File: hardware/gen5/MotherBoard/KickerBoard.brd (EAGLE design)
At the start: 141.6 x 141.1 mm, 154 parts, among them U1 SAM3S4B

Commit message: More motherboard work!
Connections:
- removed net N$39: MOTOR2.15, MOTOR2.16, MOTOR2.17, MOTOR2.18, U$8.6, U$8.7
- net 12VGND: now also MOTOR1.22, MOTOR1.33, MOTOR1.34, MOTOR2.15, MOTOR2.16, MOTOR2.17, MOTOR2.18, MOTOR2.22, MOTOR2.33, MOTOR2.34, MOTOR3.22, MOTOR3.33, MOTOR3.34, MOTOR4.22, MOTOR4.33, MOTOR4.34, U$10.5, U$11.5, U$8.6, U$8.7, U$9.5
- net GND: no longer MOTOR1.22, MOTOR1.33, MOTOR1.34, MOTOR2.22, MOTOR2.33, MOTOR2.34, MOTOR3.22, MOTOR3.33, MOTOR3.34, MOTOR4.22, MOTOR4.33, MOTOR4.34, U$10.5, U$11.5, U$9.5
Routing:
- net FAULT0: track 0.00 -> 109.2 mm, vias 0 -> 4
- net FAULT3: track 0.00 -> 106.2 mm, vias 0 -> 6
- net DIR0: track 0.00 -> 103.3 mm, vias 0 -> 4
- net 3.3V: track 274.5 -> 370.2 mm, vias 0 -> 6
- net BREN0: track 0.00 -> 76.9 mm, vias 0 -> 2
- net DIR1: track 0.00 -> 75.6 mm, vias 0 -> 2
- net GND: track 123.5 -> 186.3 mm, vias 13 -> 22
- net 12VGND: track 128.2 -> 187.4 mm, vias 5 -> 9
- net BREN1: track 0.00 -> 58.3 mm, vias 0 -> 4
- net DIR2: track 0.00 -> 53.1 mm, vias 0 -> 4
- net BREN3: track 0.00 -> 47.5 mm
- net PWM0: track 0.00 -> 44.4 mm, vias 0 -> 2
- net DIVCAP: track 6.75 -> 47.0 mm, vias 0 -> 4
- net DIR3: track 0.00 -> 38.5 mm
- net PWM3: track 0.00 -> 37.7 mm
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
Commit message: More Motherboard layout progress
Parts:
- moved C27 2.09 mm to (55.2, 46.0)
- moved C22 2.09 mm to (51.9, 46.4)
- moved C24 2.09 mm to (50.2, 46.4)
- moved C25 2.09 mm to (48.5, 46.4)
- moved C26 2.09 mm to (53.5, 46.0)
- moved R34 0.10 mm to (82.8, 48.0)
- moved R35 0.05 mm to (82.8, 50.1)
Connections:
- removed net M0QA: U1.42
- removed net M0QB: U1.41
- removed net M1QA: U1.37
- removed net M1QB: U1.38
- removed net M2QA: U1.25
- removed net M2QB: U1.26
- removed net M3QA: U1.52
- removed net M3QB: U1.23
- net M1QA-1: now also U1.25
- net M1QA-2: now also U1.37
- net M1QA-3: now also U1.42
- net M1QA-4: now also U1.52
- net M1QB-1: now also U1.26
- net M1QB-2: now also U1.38
- net M1QB-3: now also U1.41
- net M1QB-4: now also U1.23
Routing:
- net M1QA-2: track 0.00 -> 57.4 mm, vias 0 -> 4
- net M1QB-2: track 0.00 -> 55.3 mm, vias 0 -> 4
- net M1QB-3: track 0.00 -> 24.4 mm, vias 0 -> 2
- net FAULT: track 0.00 -> 23.0 mm, vias 0 -> 2
- net M1QA-3: track 0.00 -> 21.4 mm, vias 0 -> 2
- net 3.3V: track 370.2 -> 377.3 mm
- net PWM2: track 34.1 -> 40.4 mm
- net BREN2: track 37.6 -> 40.9 mm
- net TWCK: track 8.08 -> 10.6 mm
- net TWD: track 8.14 -> 9.15 mm

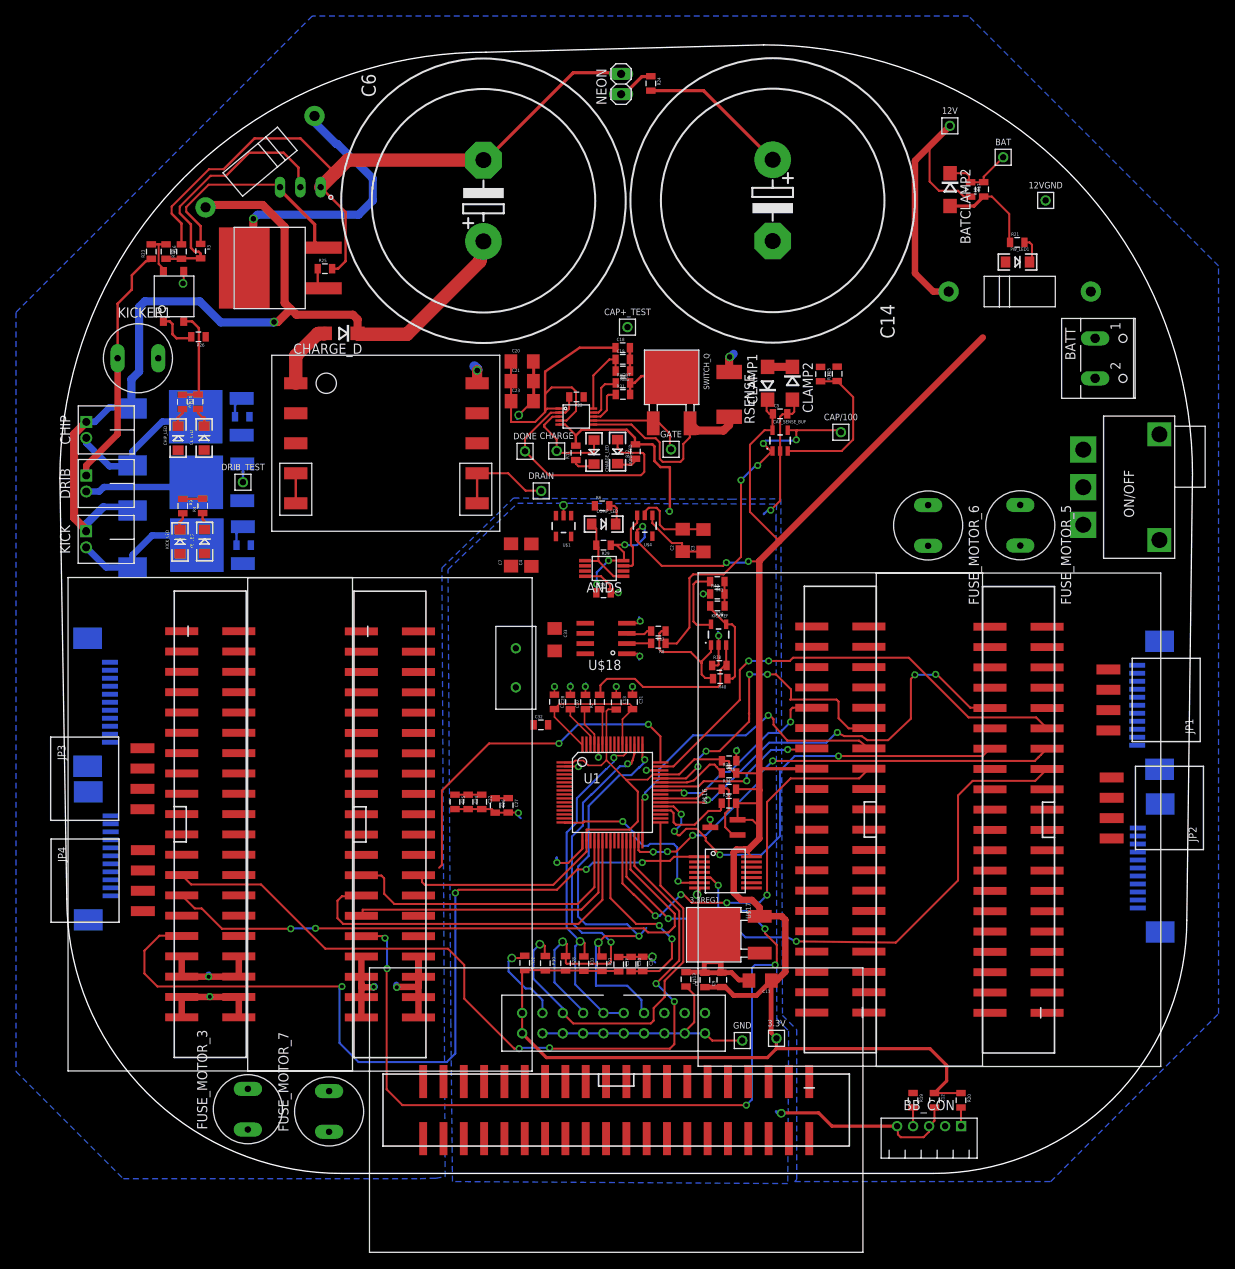
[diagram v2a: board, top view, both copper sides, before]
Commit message: Finishing up layout out traces for MCU on Motherboard
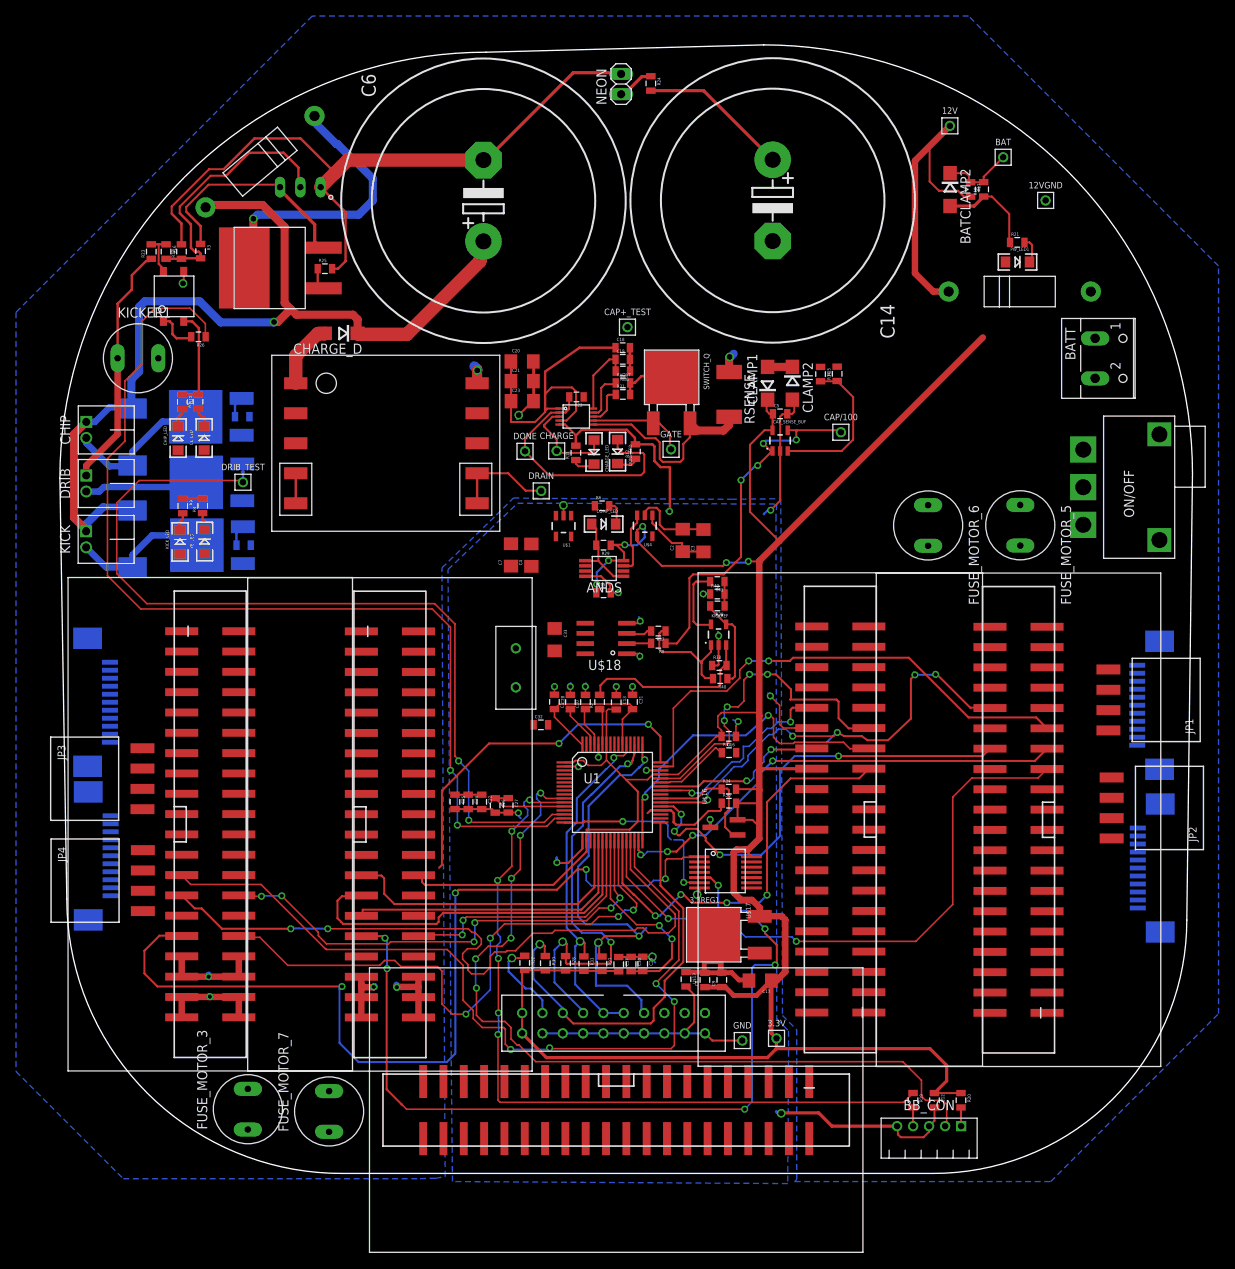
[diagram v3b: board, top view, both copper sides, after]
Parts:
- moved C16 3.05 mm to (82.7, 54.6)
- moved R35 2.54 mm to (82.8, 52.6)
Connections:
- net TWCK: now also COM_BOARD.17
- net TWD: now also COM_BOARD.19
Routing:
- net DISCHARGE: track 0.00 -> 129.2 mm, vias 0 -> 2
- net DRIB: track 2.33 -> 110.8 mm, vias 0 -> 2
- net BB_IN: track 0.00 -> 104.3 mm, vias 0 -> 6
- net BB_OUT: track 0.00 -> 97.2 mm, vias 0 -> 6
- net M1QB-1: track 0.00 -> 75.3 mm, vias 0 -> 4
- net M1QA-1: track 0.00 -> 61.6 mm, vias 0 -> 6
- net M1QB-4: track 0.00 -> 33.5 mm, vias 0 -> 2
- net BREN0: track 76.9 -> 88.5 mm
- net GND: track 186.3 -> 195.9 mm, vias 22 -> 23
- net VDDOUT: track 48.2 -> 57.6 mm
- net 12VGND: track 187.4 -> 178.5 mm
- net TWCK: track 10.6 -> 18.9 mm
- net FAULT0: track 109.2 -> 113.0 mm
- net 3.3V: track 377.3 -> 380.8 mm
- net M1QB-2: track 55.3 -> 58.8 mm, vias 4 -> 5
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
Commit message: Motherboard progress
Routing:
- net CHARGE: track 12.5 -> 80.8 mm, vias 0 -> 3
- net FAULT1: track 0.00 -> 60.0 mm, vias 0 -> 6
- net TWD: track 9.71 -> 69.5 mm, vias 0 -> 4
- net CHARGE_DONE: track 33.4 -> 91.3 mm, vias 0 -> 2
- net FAULT2: track 0.00 -> 51.4 mm, vias 0 -> 4
- net TWCK: track 18.9 -> 66.4 mm, vias 0 -> 2
- net M1QA-4: track 0.00 -> 41.6 mm, vias 0 -> 2
- net PWM0: track 44.4 -> 79.9 mm, vias 2 -> 4
- net VDDOUT: track 57.6 -> 78.9 mm, vias 2 -> 4
- net N$34: track 3.34 -> 14.6 mm
- net TDO: track 57.3 -> 52.4 mm
- net BREN1: track 58.8 -> 62.4 mm
- net TDI: track 52.0 -> 55.3 mm
- net BREN2: track 42.0 -> 44.1 mm
- net M1QB-1: track 75.3 -> 73.7 mm
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
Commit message: More motherboard Progress
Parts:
- moved FUSE_MOTOR_3 64.4 mm to (4.83, 69.9), turned to 0 degrees
- moved FUSE_MOTOR_7 62.3 mm to (29.1, 70.0), turned to 0 degrees
- moved C32 0.71 mm to (59.2, 55.4)
- moved C10 0.51 mm to (64.8, 59.4)
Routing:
- net 12V: track 79.4 -> 385.1 mm
- net GND: track 197.3 -> 304.8 mm, vias 23 -> 32
- net 3.3V: track 380.4 -> 485.1 mm, vias 8 -> 11
- net N$63: track 0.00 -> 61.0 mm, vias 0 -> 1
- net N$25: track 0.00 -> 60.4 mm
- net N$64: track 0.00 -> 58.1 mm, vias 0 -> 1
- net N$62: track 0.00 -> 57.6 mm, vias 0 -> 1
- net N$27: track 0.00 -> 55.9 mm
- net CHIP_ENABLE: track 0.00 -> 55.1 mm, vias 0 -> 2
- net M1QB-4: track 33.5 -> 88.4 mm, vias 2 -> 4
- net N$66: track 0.00 -> 47.4 mm, vias 0 -> 1
- net N$69: track 0.00 -> 45.2 mm, vias 0 -> 1
- net KICK_ENABLE: track 0.00 -> 44.3 mm, vias 0 -> 4
- net M1QA-4: track 41.6 -> 84.4 mm, vias 2 -> 4
- net N$68: track 0.00 -> 42.8 mm, vias 0 -> 1
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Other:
- board size 141.6 x 141.1 mm -> 141.6 x 142.1 mm

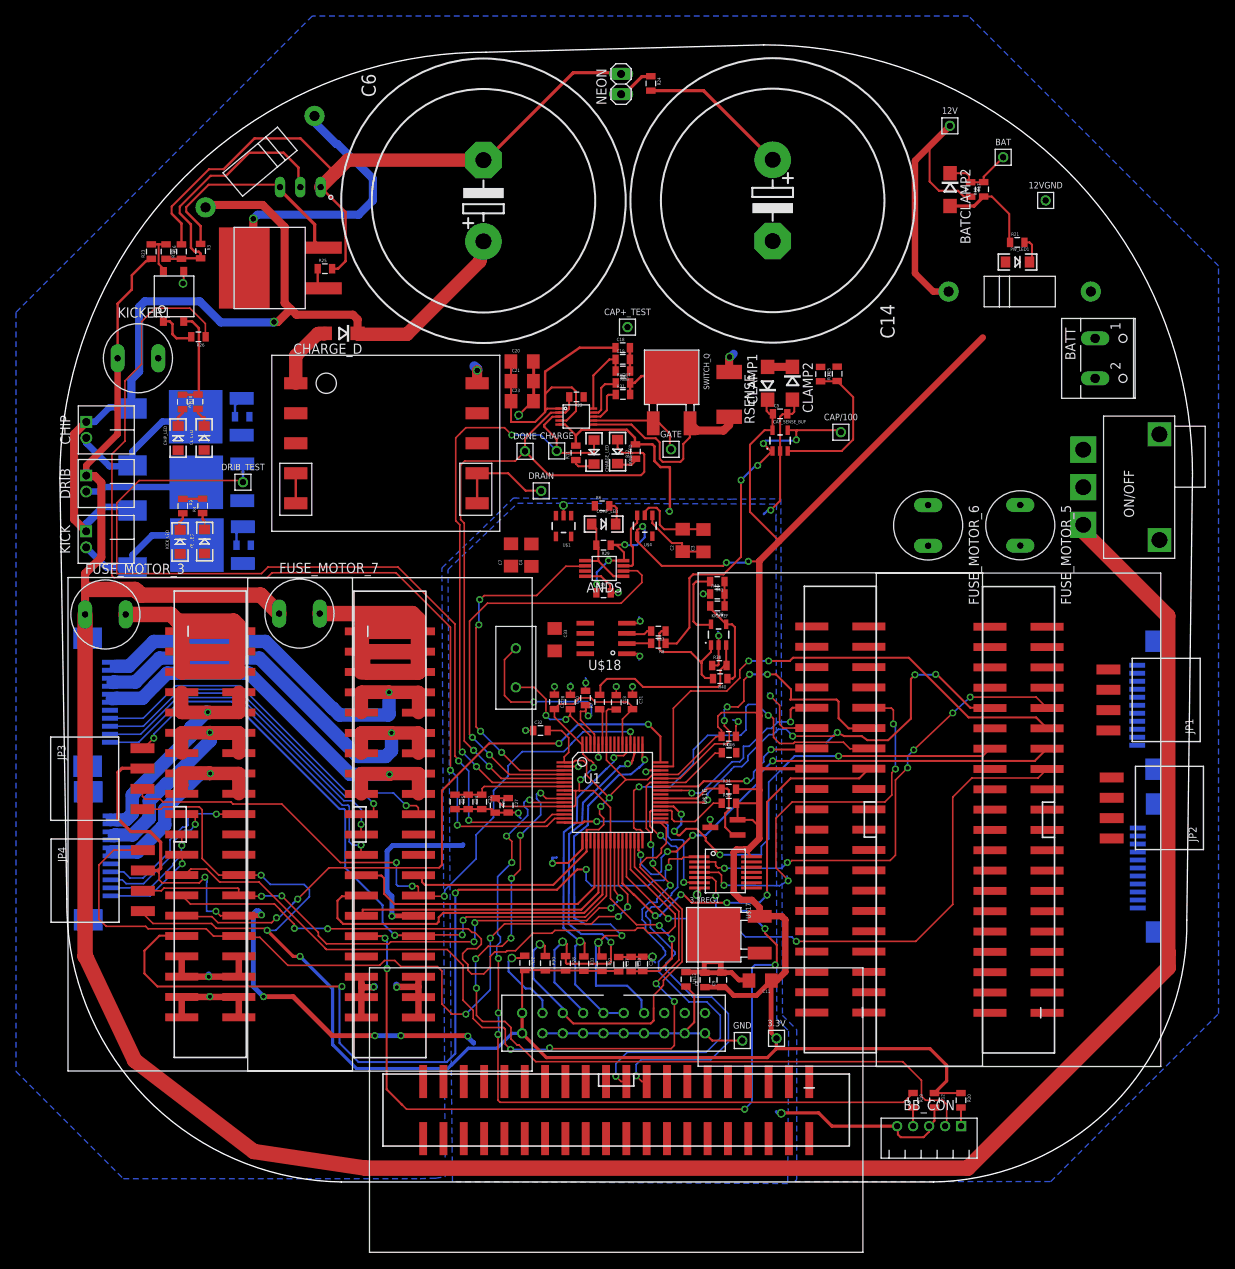
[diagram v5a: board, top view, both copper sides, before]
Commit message: Motherboard Layout needs review, design rule checking, and new header for comms board. Other than that, the layout is done.
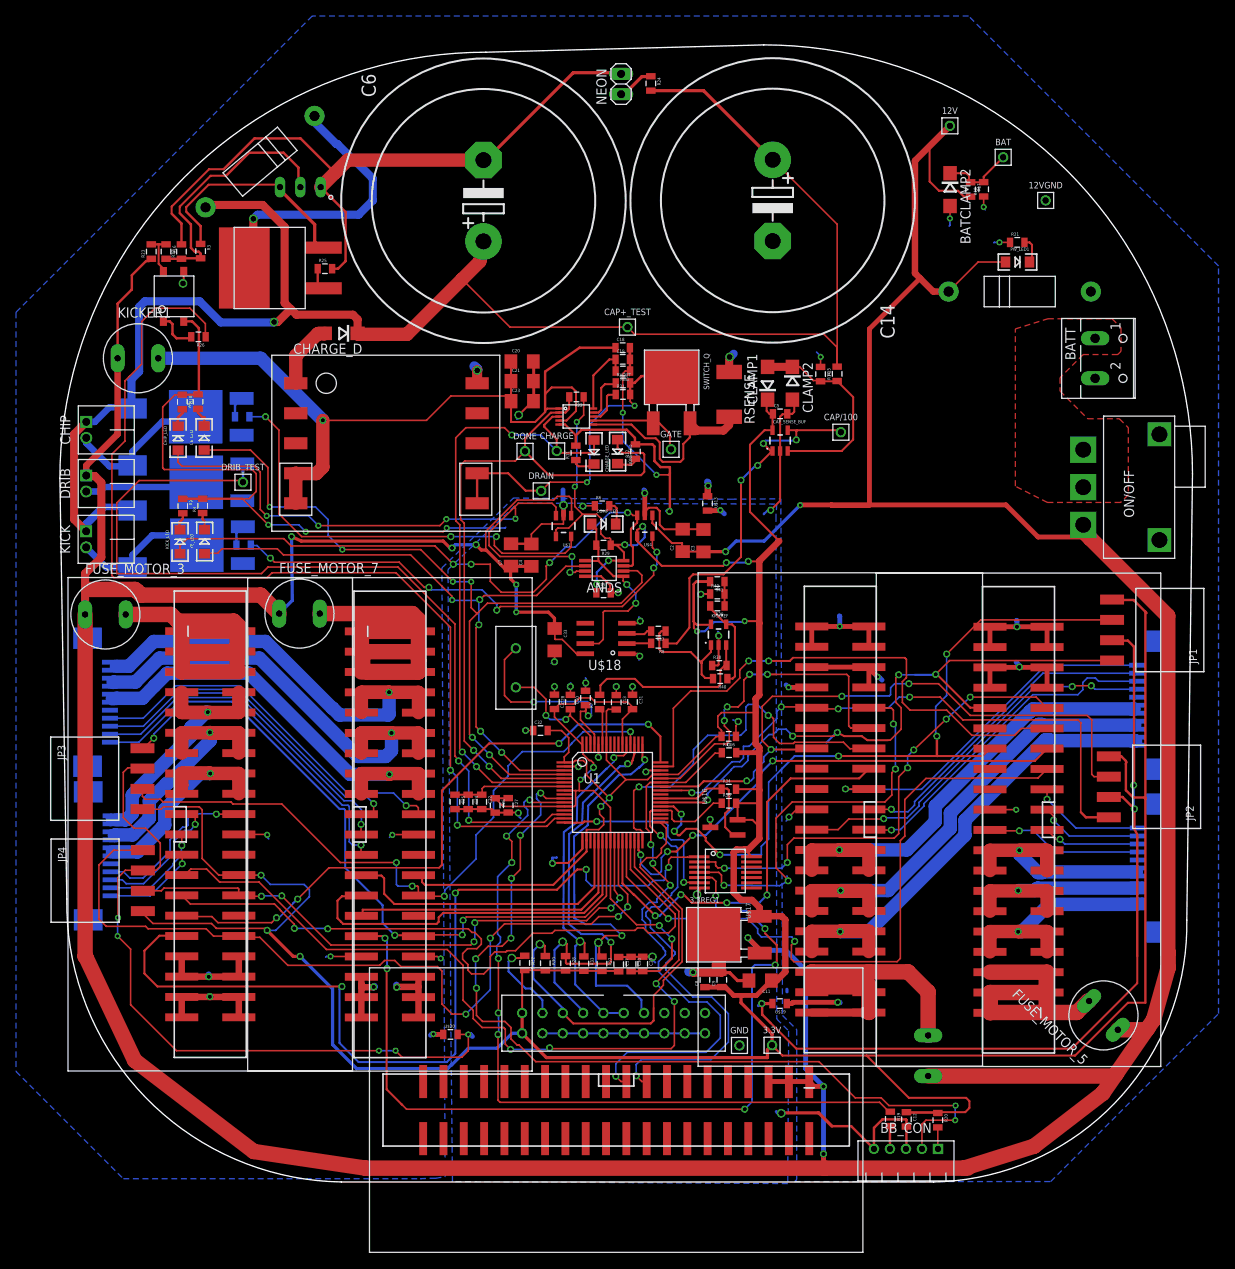
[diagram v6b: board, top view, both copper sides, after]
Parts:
- added U$19, U$20: INDUCTOR, gen3:0805
- moved FUSE_MOTOR_6 66.3 mm to (107.7, 14.7), flipped to the bottom, turned to 90 degrees
- moved FUSE_MOTOR_5 62.1 mm to (129.6, 19.8), turned to 135 degrees
- moved U$13 59.5 mm to (80.1, 83.8)
- moved JP1 8.75 mm to (137.9, 67.9)
- moved C12 4.24 mm to (105.0, 6.76)
- moved BB_CON 4.06 mm to (104.9, 3.06)
- moved R20 3.82 mm to (108.9, 6.66)
- moved R19 3.68 mm to (102.9, 6.82)
- moved JP2 2.67 mm to (137.5, 48.3)
- moved 3.3V 1.03 mm to (88.2, 16.0)
- moved GND 0.71 mm to (84.1, 16.0)
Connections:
- new net N$28: MOTOR2.15, MOTOR2.16, MOTOR2.17, MOTOR2.18, U$8.6, U$8.7
- net 12V: now also PW_LED1.A
- net 12VGND: now also BATCLAMP2.A, R18.1, R21.1, U$19.1, U$20.1, U$8.5; no longer 3.3REG1.DRAIN, C11.2, C8.2, C9.2, MOTOR2.15, MOTOR2.16, MOTOR2.17, MOTOR2.18, U$8.6, U$8.7
- net 3.3V: no longer MOTOR1.26, MOTOR2.26, MOTOR3.26, MOTOR4.26, PW_LED1.A
- net GND: now also 3.3REG1.DRAIN, C11.2, C8.2, C9.2, U$19.2, U$20.2; no longer BATCLAMP2.A, MOTOR1.30, MOTOR2.30, MOTOR3.30, MOTOR4.30, R18.1, R21.1, U$8.5
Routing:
- net 12V: track 385.1 -> 643.6 mm, vias 0 -> 10
- net GND: track 304.8 -> 472.4 mm, vias 32 -> 40
- net 3.3V: track 485.1 -> 588.4 mm, vias 11 -> 15
- net 12VGND: track 178.5 -> 273.2 mm, vias 9 -> 28
- net CAP+: track 136.8 -> 218.8 mm
- net AND_CHIP: track 0.00 -> 79.4 mm, vias 0 -> 6
- net N$54: track 0.00 -> 68.5 mm, vias 0 -> 1
- net AND_KICK: track 7.84 -> 75.7 mm, vias 0 -> 4
- net N$55: track 0.00 -> 63.6 mm, vias 0 -> 1
- net N$56: track 0.00 -> 62.5 mm, vias 0 -> 1
- net N$2: track 0.00 -> 61.2 mm, vias 0 -> 5
- net M1QA-3: track 21.8 -> 81.5 mm, vias 2 -> 4
- net 12V-KICKER: track 42.3 -> 100.6 mm, vias 0 -> 1
- net N$5: track 0.00 -> 56.1 mm, vias 0 -> 3
- net M1QB-3: track 25.2 -> 75.5 mm, vias 2 -> 4
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- added copper zone on layer 1, net BAT+
